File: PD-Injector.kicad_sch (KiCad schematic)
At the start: 10 parts

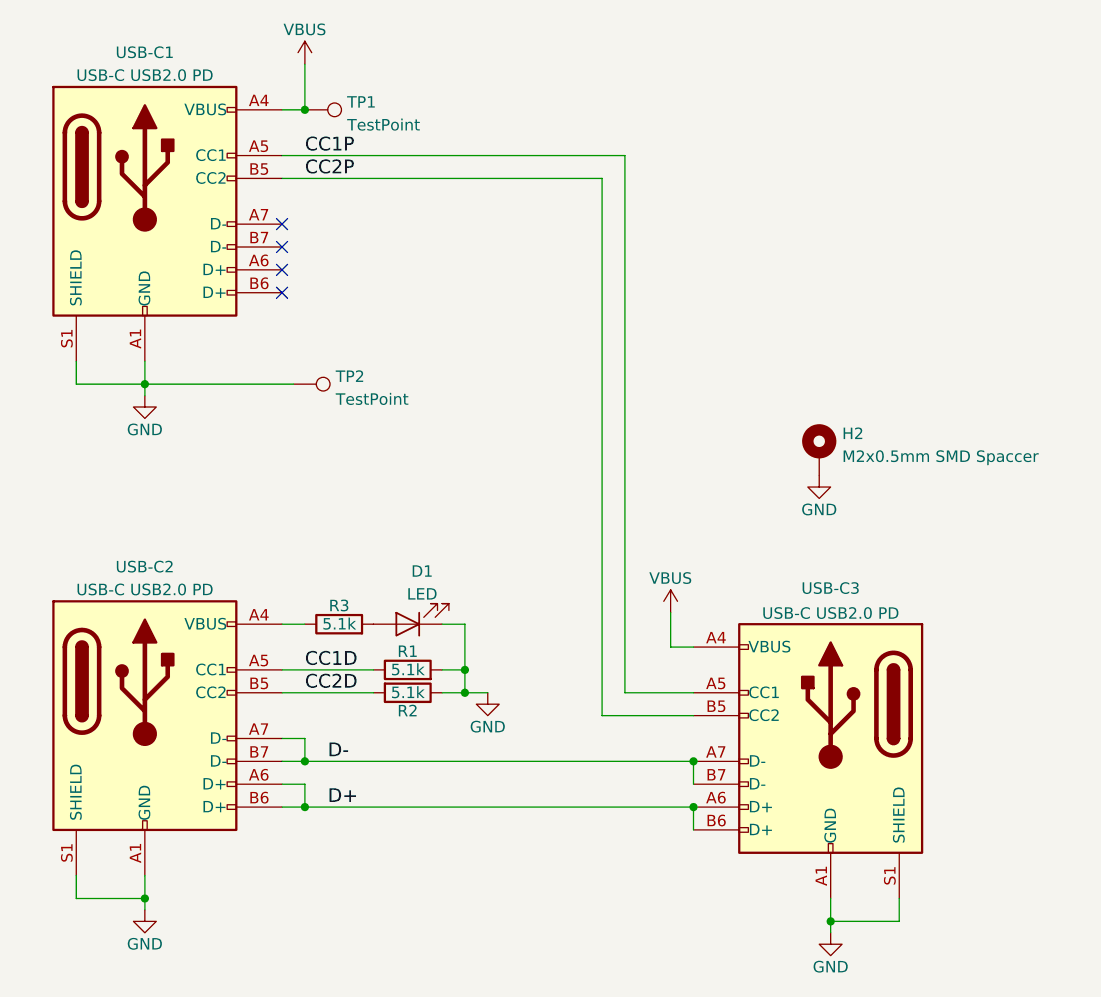
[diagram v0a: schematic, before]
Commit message: switch USB-C part
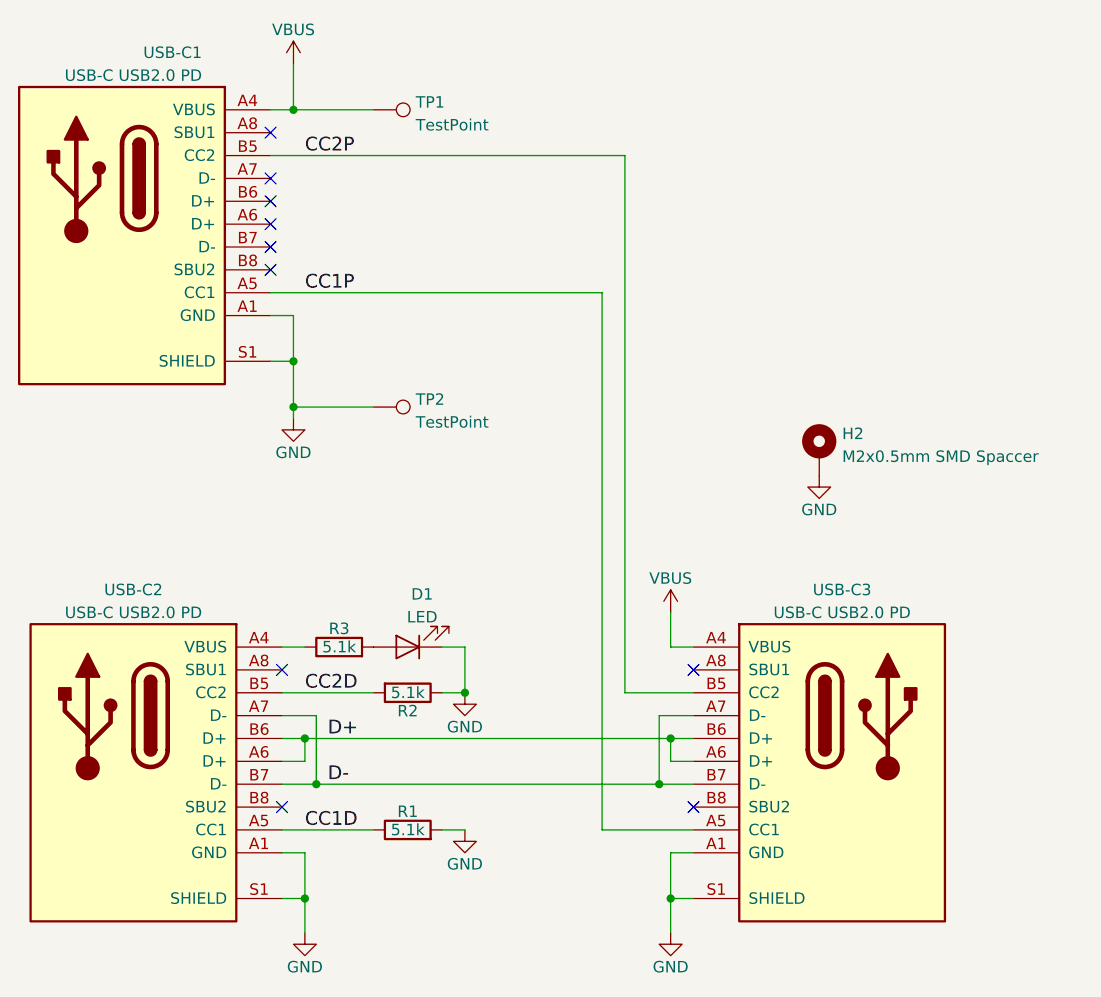
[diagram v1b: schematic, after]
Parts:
- removed USB-C1: USB-C USB2.0 PD, PD-Injector_SMD:USB_C_Receptacle_GT-USB-7010, symbol PD-Injector-SMD:USB_C_Receptacle_USB2.0
- added USB-C1: USB-C USB2.0 PD, PD-Injector:JAE_DX07S016JA1R1500, symbol PD-Injector:JAE_DX07S016JA1R1500
- USB-C2, USB-C3: footprint PD-Injector_SMD:USB_C_Receptacle_GT-USB-7010 -> PD-Injector:JAE_DX07S016JA1R1500; symbol PD-Injector-SMD:USB_C_Receptacle_USB2.0 -> PD-Injector:JAE_DX07S016JA1R1500
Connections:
- net CC1P: now also USB-C1.A5 (CC1)
- net CC2P: now also USB-C1.B5 (CC2)
- net GND: now also USB-C2.S2 (SHIELD), USB-C2.S3 (SHIELD), USB-C2.S4 (SHIELD), USB-C2.S5 (SHIELD), USB-C2.S6 (SHIELD), USB-C3.S2 (SHIELD), USB-C3.S3 (SHIELD), USB-C3.S4 (SHIELD), USB-C3.S5 (SHIELD), USB-C3.S6 (SHIELD), USB-C1.A1 (GND), USB-C1.A12 (GND), USB-C1.B1 (GND), USB-C1.B12 (GND), USB-C1.S1 (SHIELD), USB-C1.S2 (SHIELD), USB-C1.S3 (SHIELD), USB-C1.S4 (SHIELD), USB-C1.S5 (SHIELD), USB-C1.S6 (SHIELD)
- net VBUS: now also USB-C1.A4 (VBUS), USB-C1.A9 (VBUS), USB-C1.B4 (VBUS), USB-C1.B9 (VBUS)
- no-connect marks 4 -> 10
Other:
- title: PD-injector-SMD -> PD-injector
- moved on the sheet: D1, R3, TP1, TP2

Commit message: more vbus copper
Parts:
- H2, TP1, TP2: now left out of the parts list
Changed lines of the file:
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@@
   )
   (symbol (lib_id "Connector:TestPoint") (at 124.46 90.17 270) (unit 1)
-    (in_bom yes) (on_board yes) (dnp no) (fields_autoplaced)
+    (in_bom no) (on_board yes) (dnp no) (fields_autoplaced)
     (property "Reference" "TP2" (at 129.159 89.3353 90)
       (effects (font (size 1.27 1.27)) (justify left))
@@
   )
   (symbol (lib_id "Connector:TestPoint") (at 124.46 57.15 270) (unit 1)
-    (in_bom yes) (on_board yes) (dnp no) (fields_autoplaced)
+    (in_bom no) (on_board yes) (dnp no) (fields_autoplaced)
     (property "Reference" "TP1" (at 129.159 56.3153 90)
       (effects (font (size 1.27 1.27)) (justify left))
@@
   )
   (symbol (lib_id "Mechanical:MountingHole_Pad") (at 173.99 95.25 0) (unit 1)
-    (in_bom yes) (on_board yes) (dnp no) (fields_autoplaced)
+    (in_bom no) (on_board yes) (dnp no) (fields_autoplaced)
     (property "Reference" "H2" (at 176.53 93.1453 0)
       (effects (font (size 1.27 1.27)) (justify left))
